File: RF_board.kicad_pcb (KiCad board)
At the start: 2 copper layers, 89.4 x 41.4 mm, 2 parts, among them J1 Conn_Coaxial, U1 SPF5189Z

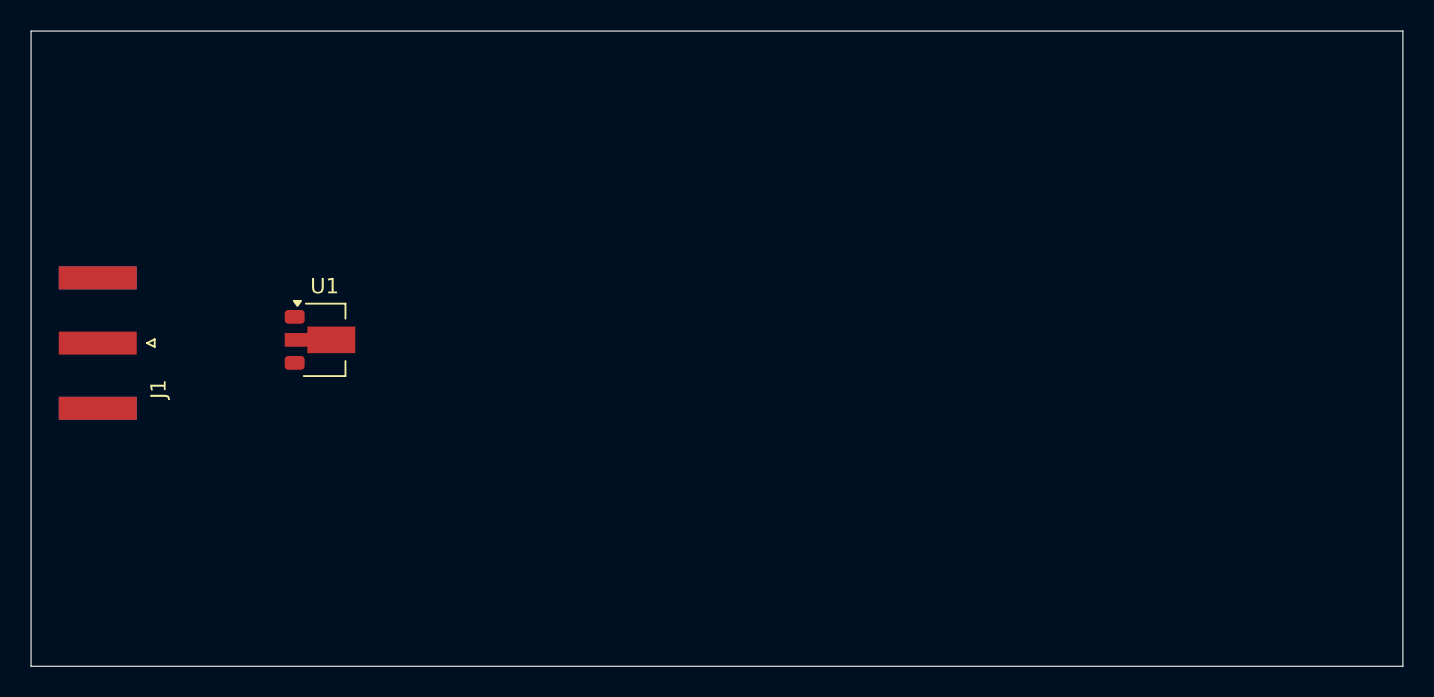
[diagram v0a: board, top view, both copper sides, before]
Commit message: added ground stitching vias to SMA connector
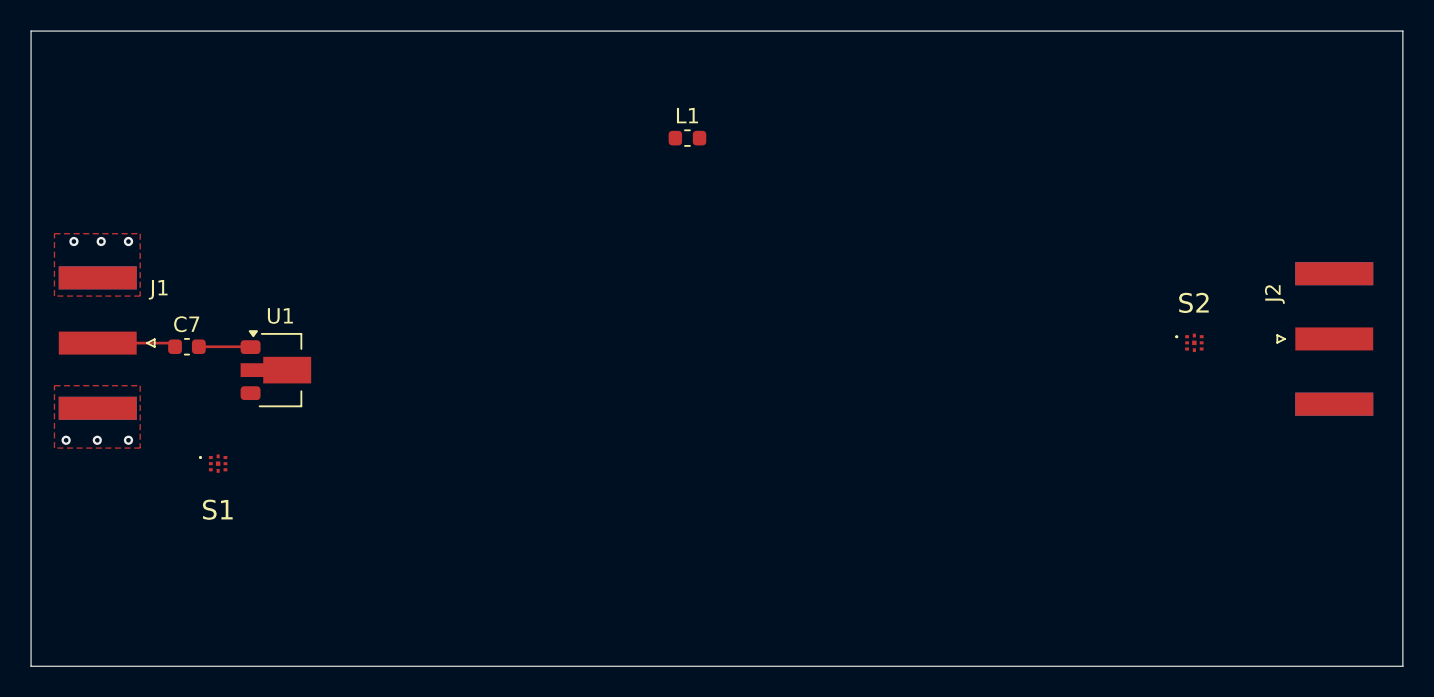
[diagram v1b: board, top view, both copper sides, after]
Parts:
- added C7: 1n, Capacitor_SMD:C_0603_1608Metric, F.Cu at (98.0, 115.8)
- added J2: Conn_Coaxial, Connector_Coaxial:SMA_Amphenol_132289_EdgeMount, F.Cu at (172.8, 115.3)
- added L1: 6.2n, Inductor_SMD:L_0603_1608Metric, F.Cu at (130.7, 102.2)
- added S1: SKY13586-678LF, RF_board_footprints:SKY13586678LF, F.Cu at (100.1, 123.4)
- added S2: SKY13586-678LF, RF_board_footprints:SKY13586678LF, F.Cu at (163.7, 115.6)
- moved U1 3.49 mm to (104.1, 117.3)
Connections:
- J1 pad 1: GND -> /RF_in
- J1 pad 2: Net-(J1-Ext) -> GND
- U1 pad 1: Net-(J1-Ext) -> /RF_decop
- U1 pad 3: unconnected-(U1-Pad3) -> /RF_amped
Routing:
- net /RF_in: track 0.00 -> 5.14 mm
- net /RF_decop: track 0.00 -> 3.38 mm
- net GND: track 0.00 -> 1.72 mm, vias 0 -> 6
- added copper zone on F.Cu, net GND
- added copper zone on In1.Cu, net GND
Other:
- copper layers 2 -> 4
